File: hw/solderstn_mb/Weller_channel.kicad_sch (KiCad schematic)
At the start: 42 parts, among them U1501 AD8552ARU, U1502 INA226, U1503 TPS2HB16AQ1, U1504 INA226, U1505 74LVC1G11dck, U1506 74LVC1G11dck, U1507 74LVC1G11dck

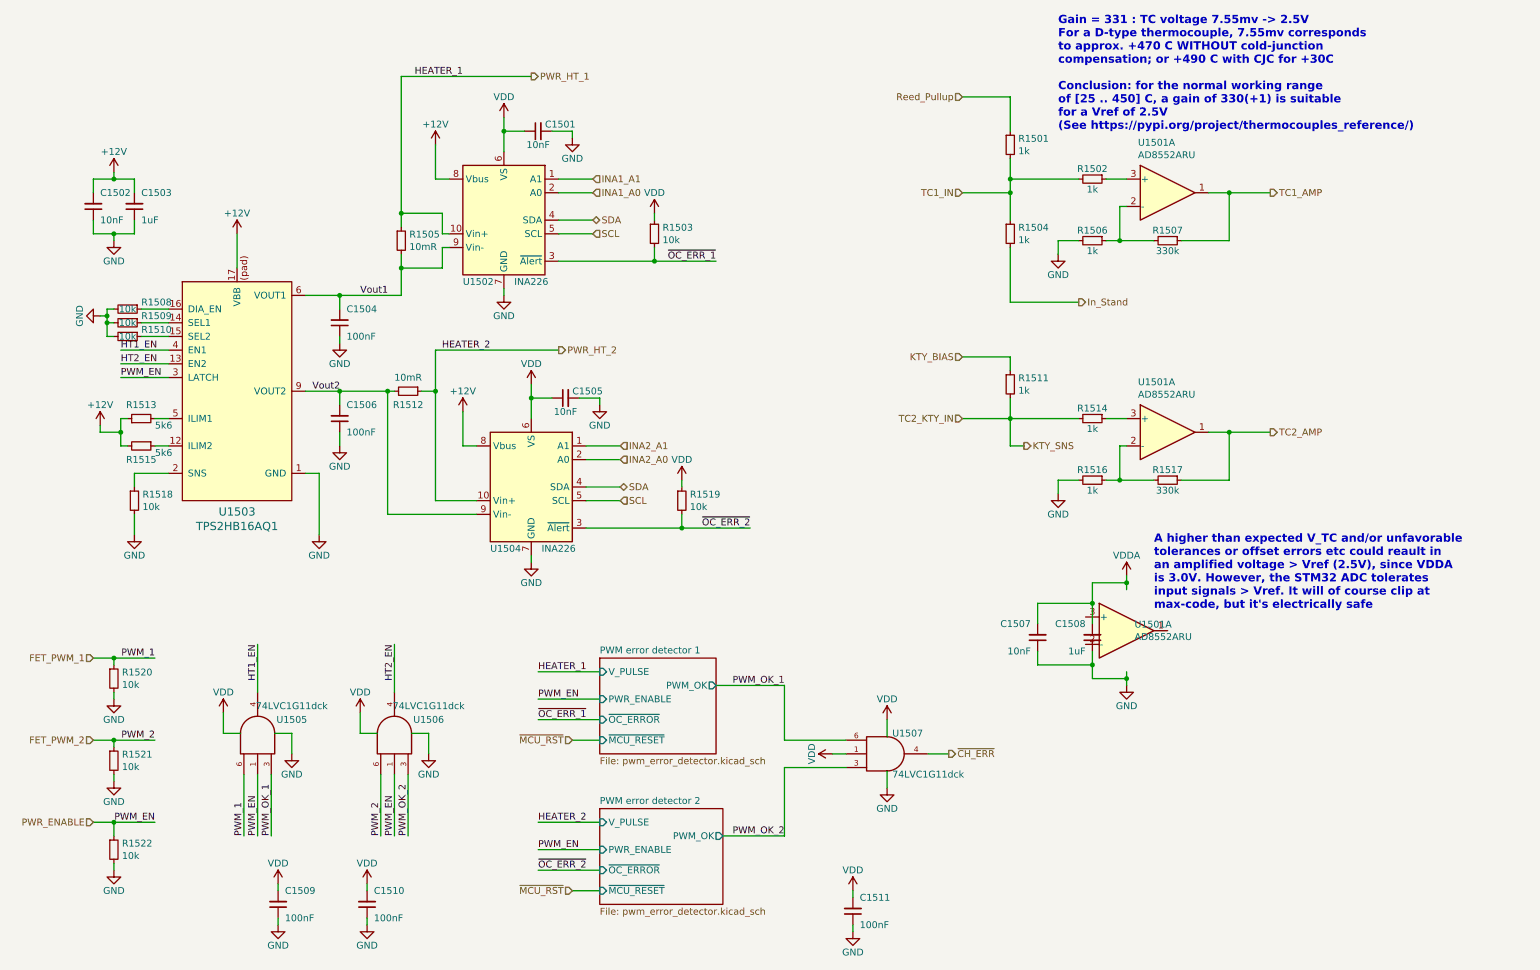
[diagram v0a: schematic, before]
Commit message: solderstn_mb::power - changed generic 2x2 connector to customlib_mj:Molex_MicroFit 2x2
(and a whole bunch of other automatic changes, crap)
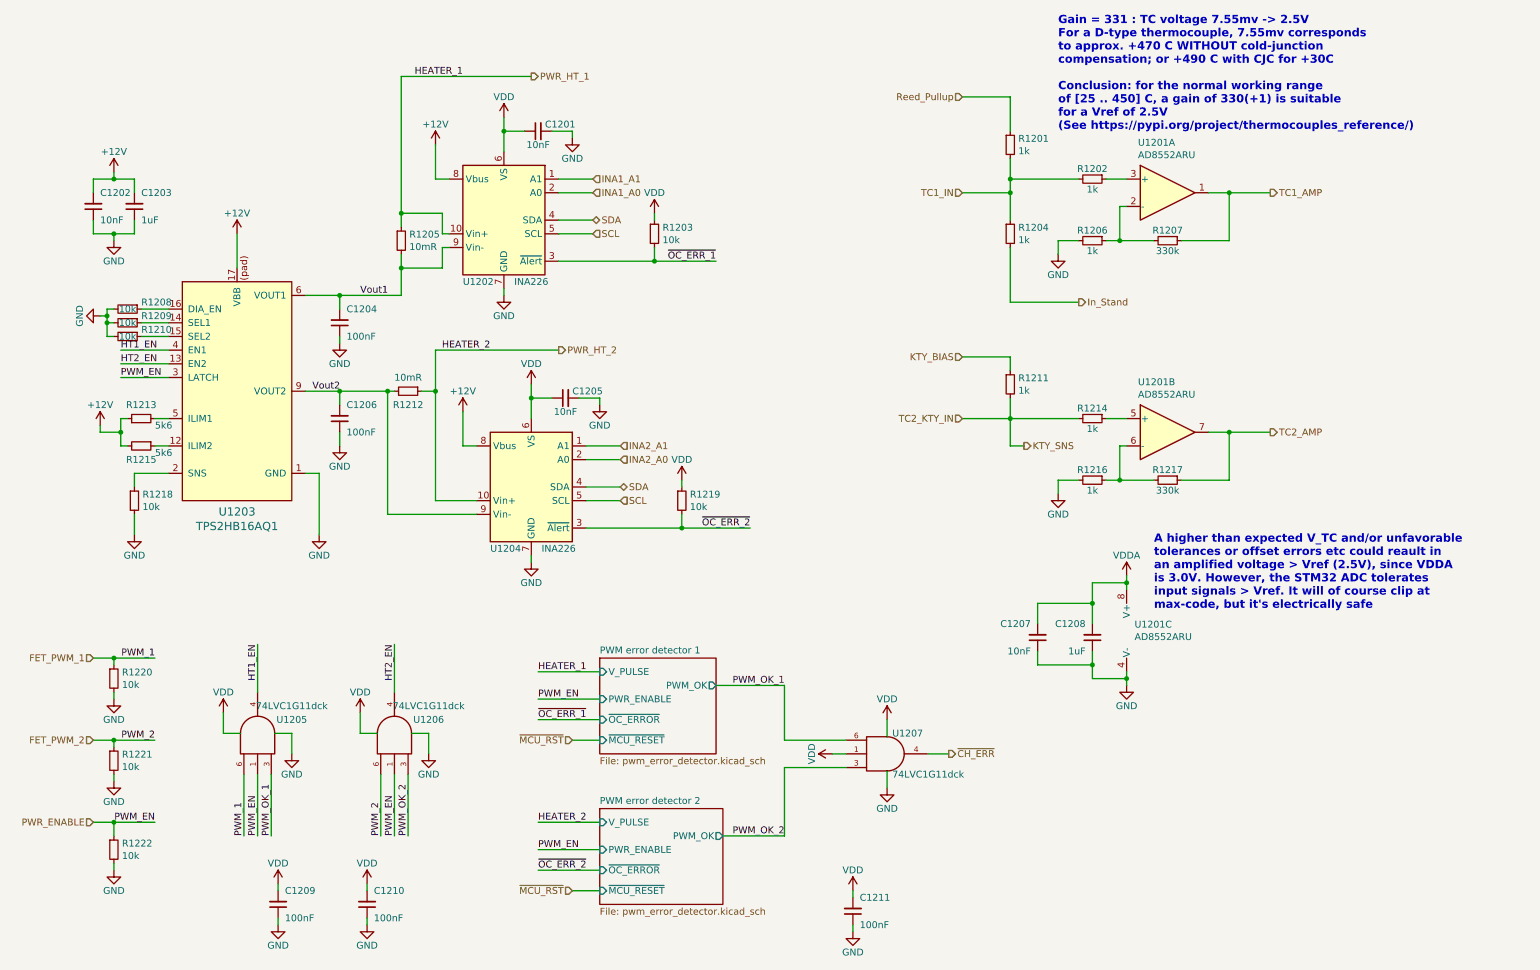
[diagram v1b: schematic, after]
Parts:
- renumbered C1501 to C1201, C1502 to C1202, C1503 to C1203, C1504 to C1204, C1505 to C1205, C1506 to C1206, C1507 to C1207, C1508 to C1208, C1509 to C1209, C1510 to C1210, C1511 to C1211, R1501 to R1201, R1502 to R1202, R1503 to R1203, R1504 to R1204, R1505 to R1205, R1506 to R1206, R1507 to R1207, R1508 to R1208, R1509 to R1209, R1510 to R1210, R1511 to R1211, R1512 to R1212, R1513 to R1213, R1514 to R1214, R1515 to R1215, R1516 to R1216, R1517 to R1217, R1518 to R1218, R1519 to R1219, R1520 to R1220, R1521 to R1221, R1522 to R1222, U1501 to U1201, U1502 to U1202, U1503 to U1203, U1504 to U1204, U1505 to U1205, U1506 to U1206, U1507 to U1207
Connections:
- net GND: now also U1201.4 (V-)
- net TC2_AMP: now also U1201.7; no longer U1201.1
- net VDDA: now also U1201.8 (V+)
- net at R1216.1, R1217.2: now also U1201.6 (-); no longer U1201.2 (-)
- net at R1214.1: now also U1201.5 (+); no longer U1201.3 (+)

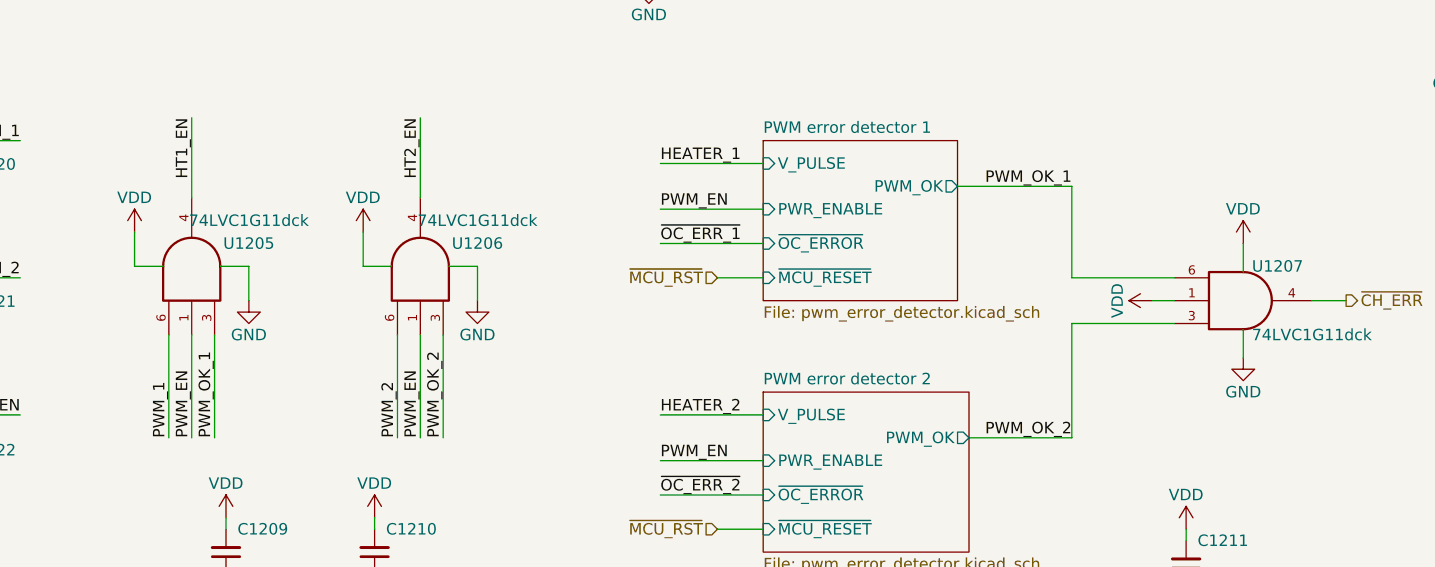
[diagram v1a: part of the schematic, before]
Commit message: hw: long-standing uncommitted stuff; mostly auto-updates (v7) fw: remove L052 tree (CMSIS & std-HAL shouldn't be committed and it was the wrong device name anyway)
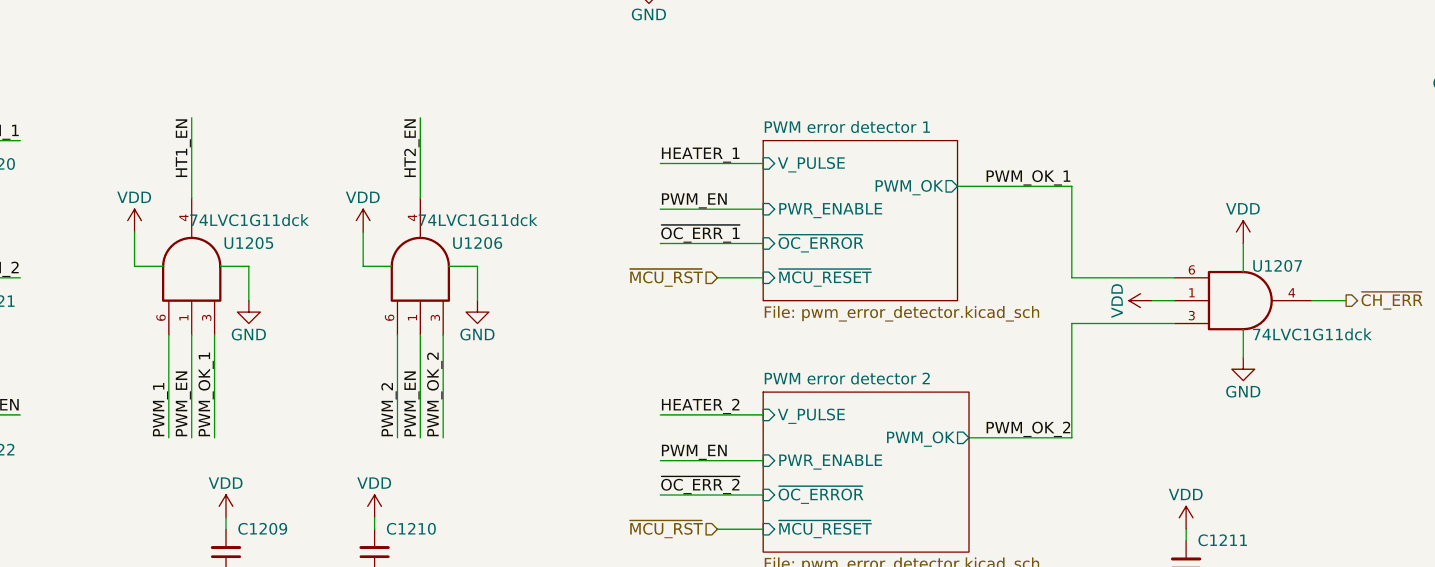
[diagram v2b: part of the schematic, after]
